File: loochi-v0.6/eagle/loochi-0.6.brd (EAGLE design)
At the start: 68.8 x 63.8 mm, 51 parts, among them IC1 ATTINY61M, J1 SPI_PRG, J2 POWER_JACKSMT3, P1 53047-0610, Q1 PMN25ENSOT457, Q2 PMN25ENSOT457, Q3 PMN25ENSOT457, U1 BLE112, U2 LZ4-00MC00BIGPADS, U3 LP2985

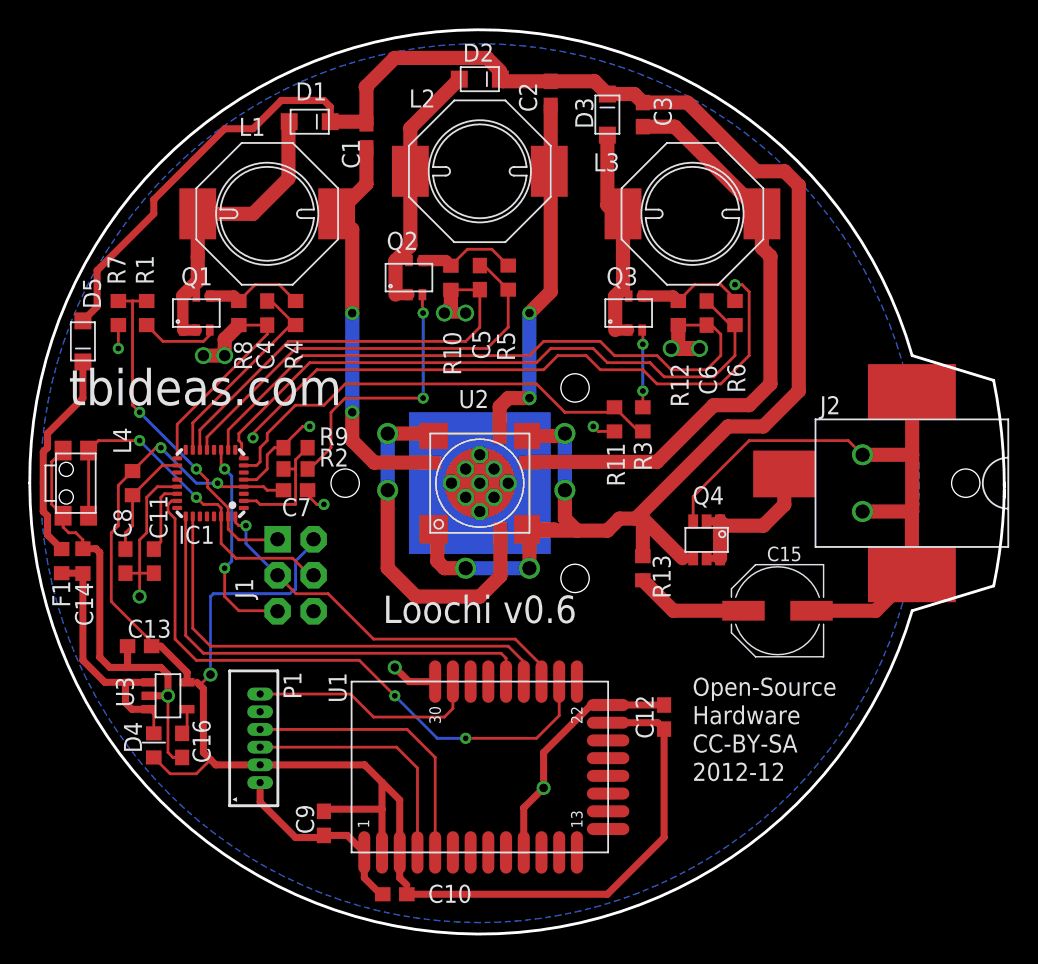
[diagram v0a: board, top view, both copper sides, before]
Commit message: One major fix (vias under the cpu removed) + minor adjustments
 * Removed all vias under the CPU
 * Fix holes for the lense
 * Fix size of power supply tab
 * Connect the button to the BLE Module
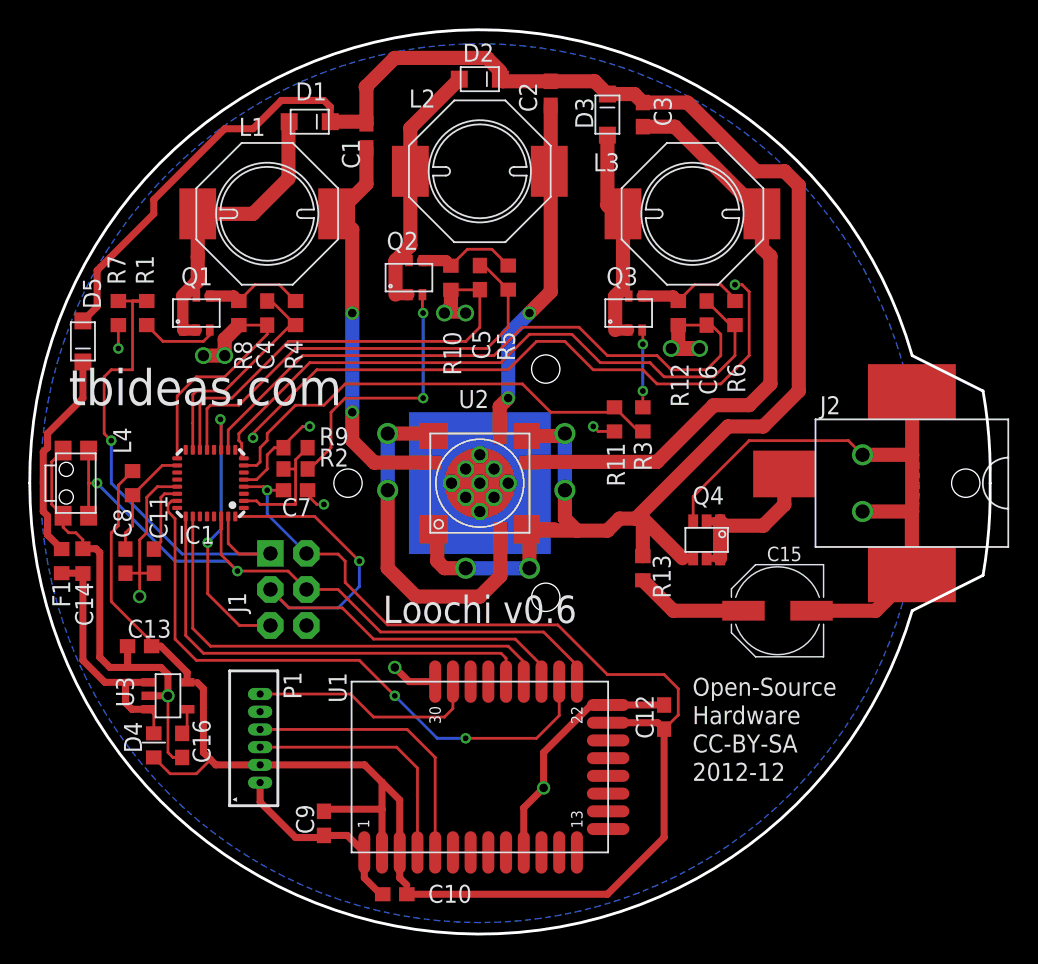
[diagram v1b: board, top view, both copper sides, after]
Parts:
- moved J1 1.12 mm to (18.5, 24.5)
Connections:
- net BUTTON/MOSI: now also U1.P0_6
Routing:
- net BUTTON/MOSI: track 26.6 -> 51.1 mm
- net BLE-CS/SCK: track 28.1 -> 41.8 mm
- net VCC: track 121.1 -> 134.5 mm, vias 3 -> 1
- net RPWM/MISO: track 24.7 -> 36.3 mm, vias 2 -> 1
- net RESET: track 15.2 -> 20.3 mm
- net GND: track 288.3 -> 292.3 mm
- net RSENSE: track 14.7 -> 15.9 mm
- net GSENSE: track 30.7 -> 31.9 mm
- net GREENC: track 25.6 -> 24.7 mm
- net BSENSE: track 45.7 -> 46.6 mm
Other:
- board size 68.8 x 63.8 mm -> 67.8 x 63.8 mm

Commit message: Routed connections + Added SPI on BLE connector + Some cleaning/Rework
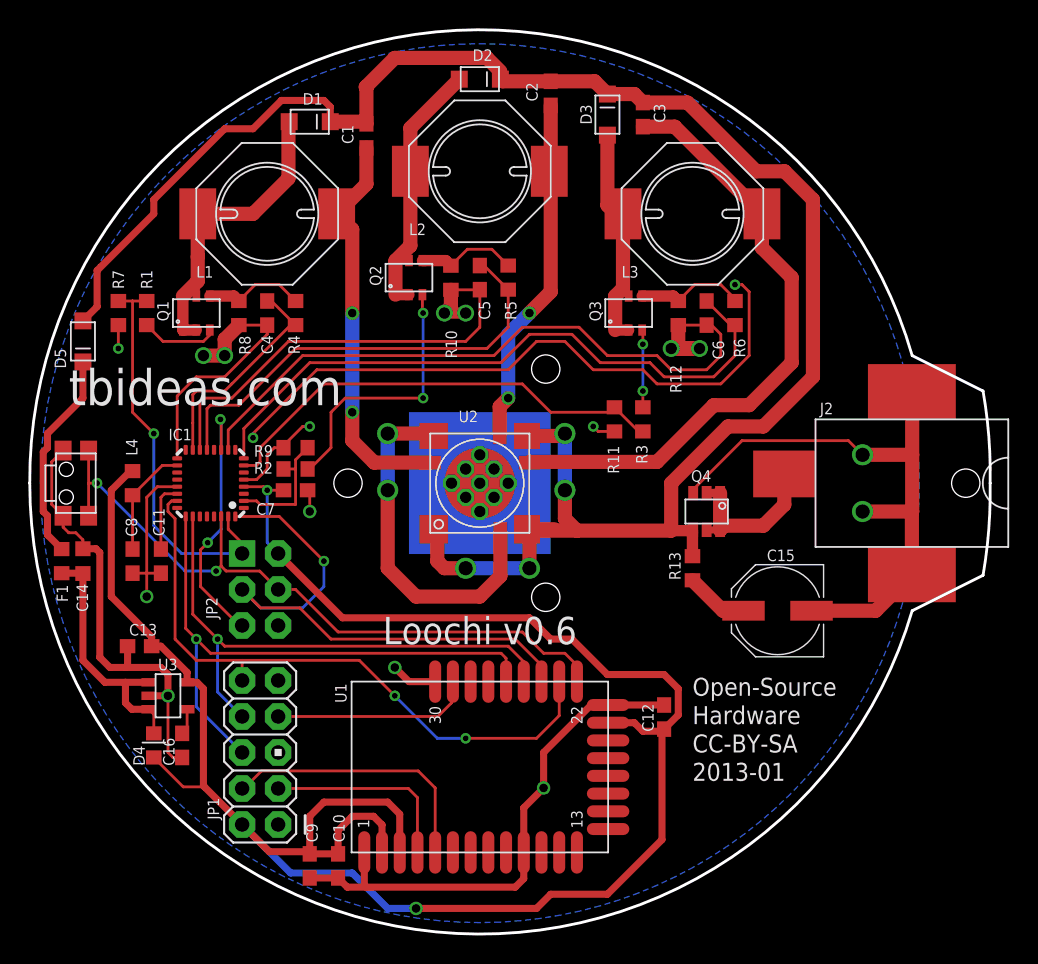
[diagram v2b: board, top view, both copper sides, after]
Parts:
- removed J1: SPI_PRG, SparkFun:2X3-NS
- removed P1: 53047-0610, con-molex-picoblade:53047-0610
- added JP1: M05X2PTH, SparkFun:AVR_ICSP
- added JP2: SPI_PRG, SparkFun:2X3-NS
- moved C10 4.47 mm to (22.0, 5.00), turned to 270 degrees
- moved R13 3.50 mm to (47.0, 26.0)
- moved C9 3.16 mm to (20.0, 5.00)
- moved Q4 2.00 mm to (48.0, 30.0)
- moved C11 0.50 mm to (9.50, 26.5)
- moved C8 0.50 mm to (7.50, 26.5)
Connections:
- net BLE-CS/SCK: now also JP2.3; no longer J1.3
- net BLE-MISO: now also JP1.6
- net BLE-MOSI: now also JP1.8
- net BLE-RESET: now also JP1.7; no longer P1.6
- net BLE-SCK: now also JP1.10
- net BUTTON/MOSI: now also JP2.4; no longer J1.4
- net GND: now also JP1.1, JP2.6; no longer J1.6, P1.1
- net P2_1: now also JP1.4; no longer P1.4
- net P2_2: now also JP1.3; no longer P1.3
- net RESET: now also JP2.5; no longer J1.5
- net RPWM/MISO: now also JP2.1; no longer J1.1
- net VCC: now also JP1.2, JP2.2; no longer J1.2, P1.2
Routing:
- net VCC: track 134.5 -> 151.3 mm, vias 1 -> 2
- net BLE-MISO: track 33.3 -> 42.4 mm, vias 0 -> 1
- net RPWM/MISO: track 36.3 -> 28.5 mm
- net BLE-MOSI: track 33.6 -> 39.2 mm, vias 0 -> 1
- net GND: track 292.3 -> 296.5 mm
- net P2_2: track 17.7 -> 14.0 mm
- net N$21: track 7.99 -> 4.70 mm
- net BLE-RESET: track 16.4 -> 14.2 mm
- net RESET: track 20.3 -> 18.7 mm
- net V+: track 137.3 -> 135.7 mm
- net BUTTON/MOSI: track 51.1 -> 49.7 mm
- net BLE-SCK: track 43.5 -> 44.9 mm
- net BLUEC: track 42.5 -> 43.7 mm
- net BLE-CS/SCK: track 41.8 -> 40.8 mm
- net P2_1: track 19.9 -> 19.2 mm
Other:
- board text added: "2013-01"
- board text removed: "2012-12"

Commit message: Final changes before ordering the board (minor cosmetic changes)
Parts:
- JP1: value M05X2PTH -> SPI_PRG; device SparkFun:AVR_ICSP -> SparkFun:2X3-NS
- JP2: value SPI_PRG -> M05X2PTH; device SparkFun:2X3-NS -> SparkFun:AVR_ICSP
- moved JP1 11.5 mm to (16.5, 24.5), turned to 270 degrees
- moved JP2 11.5 mm to (16.5, 13.0), turned to 180 degrees
- renumbered J2 to J1
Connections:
- net BLE-CS/SCK: now also JP1.3; no longer JP2.3
- net BLE-MISO: now also JP2.6; no longer JP1.6
- net BLE-MOSI: now also JP2.8; no longer JP1.8
- net BLE-RESET: now also JP2.7; no longer JP1.7
- net BLE-SCK: now also JP2.10; no longer JP1.10
- net BUTTON/MOSI: now also JP1.4; no longer JP2.4
- net GND: now also JP1.6, JP2.1; no longer JP1.1, JP2.6
- net P2_1: now also JP2.4; no longer JP1.4
- net P2_2: now also JP2.3; no longer JP1.3
- net RESET: now also JP1.5; no longer JP2.5
- net RPWM/MISO: now also JP1.1; no longer JP2.1
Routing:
- net GND: track 296.5 -> 297.1 mm

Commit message: Fixing reference of F1 (we want a 0603)
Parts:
- F1: value MPZ2012 -> MPZ1608
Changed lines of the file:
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@@
 <attribute name="NAME" x="46.165" y="25.165" size="0.8128" layer="25" rot="R90"/>
 </element>
-<element name="F1" library="rcl" package="R0603" value="MPZ2012" x="2.5" y="26.5" smashed="yes" rot="R270">
+<element name="F1" library="rcl" package="R0603" value="MPZ1608" x="2.5" y="26.5" smashed="yes" rot="R270">
 <attribute name="NAME" x="2.135" y="24.835" size="0.8128" layer="25" rot="R270"/>
 </element>
